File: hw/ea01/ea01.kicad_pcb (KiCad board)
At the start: 2 copper layers, 50 parts, among them J1 Screw_Terminal_01x02, SW1 SW_Push, U1 RP2040, U2 DS1302Z+, U3 NUP2202, U4 MC34063AD, U5 AMS1117-5.0, U6 AMS1117-3.3, U7 MCP601-xOT

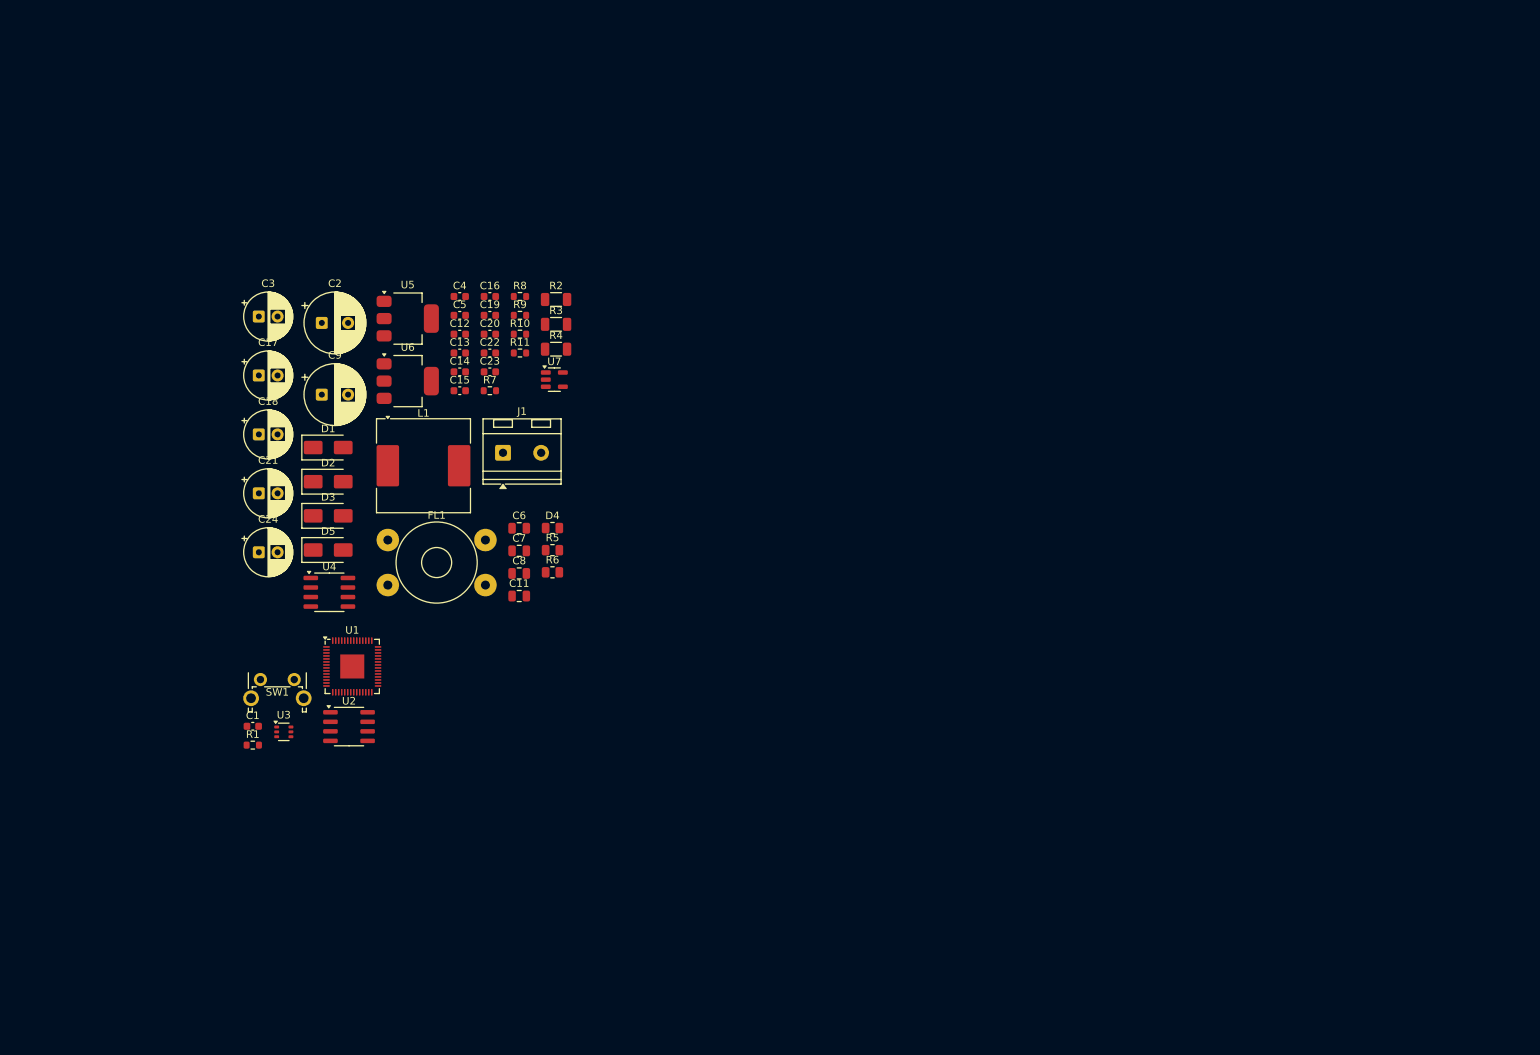
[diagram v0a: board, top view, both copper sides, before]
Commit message: errors fix for comp fp
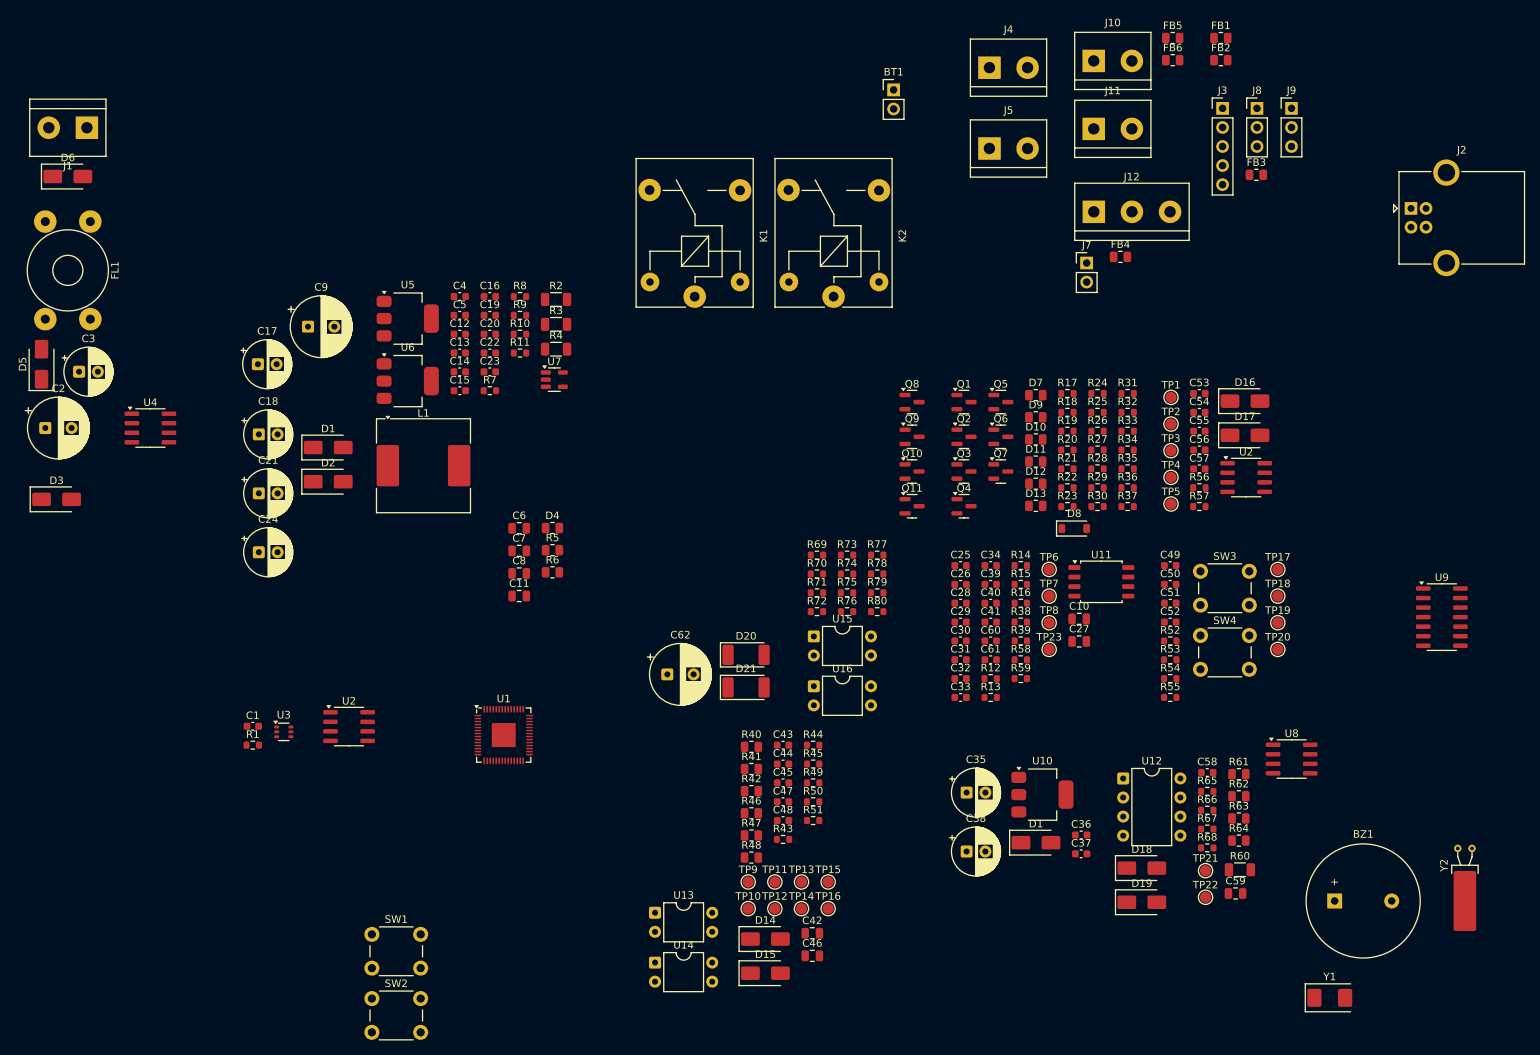
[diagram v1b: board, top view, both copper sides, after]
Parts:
- added BT1: Battery_Cell, Connector_PinHeader_2.54mm:PinHeader_1x02_P2.54mm_Vertical, F.Cu at (199.0, 31.5)
- added BZ1: Buzzer, Buzzer_Beeper:Buzzer_15x7.5RM7.6, F.Cu at (257.8, 139.5)
- added C10: 1uF, Capacitor_SMD:C_0805_2012Metric, F.Cu at (223.7, 101.9)
- added C25: 220nF, Capacitor_SMD:C_0603_1608Metric, F.Cu at (207.9, 94.8)
- added C26: 100nF, Capacitor_SMD:C_0603_1608Metric, F.Cu at (207.9, 97.3)
- added C27: 1uF, Capacitor_SMD:C_0805_2012Metric, F.Cu at (223.7, 104.9)
- added C28: 220nF, Capacitor_SMD:C_0603_1608Metric, F.Cu at (207.9, 99.8)
- added C29: 220nF, Capacitor_SMD:C_0603_1608Metric, F.Cu at (207.9, 102.3)
- added C30: 220nF, Capacitor_SMD:C_0603_1608Metric, F.Cu at (207.9, 104.9)
- added C31: 220nF, Capacitor_SMD:C_0603_1608Metric, F.Cu at (207.9, 107.4)
- added C32: 220nF, Capacitor_SMD:C_0603_1608Metric, F.Cu at (207.9, 109.9)
- added C33: 220nF, Capacitor_SMD:C_0603_1608Metric, F.Cu at (207.9, 112.4)
- added C34: 220nF, Capacitor_SMD:C_0603_1608Metric, F.Cu at (211.9, 94.8)
- added C35: 10uF, Capacitor_THT:CP_Radial_D6.3mm_P2.50mm, F.Cu at (208.7, 125.1)
- added C36: 220nF, Capacitor_SMD:C_0603_1608Metric, F.Cu at (224.0, 130.7)
- added C37: 220nF, Capacitor_SMD:C_0603_1608Metric, F.Cu at (224.0, 133.2)
- added C38: 10uF, Capacitor_THT:CP_Radial_D6.3mm_P2.50mm, F.Cu at (208.7, 132.9)
- added C39: 15pF, Capacitor_SMD:C_0603_1608Metric, F.Cu at (211.9, 97.3)
- added C40: 220nF, Capacitor_SMD:C_0603_1608Metric, F.Cu at (211.9, 99.8)
- added C41: 15pF, Capacitor_SMD:C_0603_1608Metric, F.Cu at (211.9, 102.3)
- added C42: 100nF, Capacitor_SMD:C_0805_2012Metric, F.Cu at (188.2, 143.8)
- added C43: 220nF, Capacitor_SMD:C_0603_1608Metric, F.Cu at (184.3, 118.8)
- added C44: 220nF, Capacitor_SMD:C_0603_1608Metric, F.Cu at (184.3, 121.3)
- added C45: 220nF, Capacitor_SMD:C_0603_1608Metric, F.Cu at (184.3, 123.8)
- added C46: 100nF, Capacitor_SMD:C_0805_2012Metric, F.Cu at (188.2, 146.8)
- added C47: 100nF, Capacitor_SMD:C_0603_1608Metric, F.Cu at (184.3, 126.3)
- added C48: 100nF, Capacitor_SMD:C_0603_1608Metric, F.Cu at (184.3, 128.8)
- added C49: 220nF, Capacitor_SMD:C_0603_1608Metric, F.Cu at (235.8, 94.8)
- added C50: 220nF, Capacitor_SMD:C_0603_1608Metric, F.Cu at (235.8, 97.3)
- added C51: 220nF, Capacitor_SMD:C_0603_1608Metric, F.Cu at (235.8, 99.8)
- added C52: 220nF, Capacitor_SMD:C_0603_1608Metric, F.Cu at (235.8, 102.3)
- added C53: 15pF, Capacitor_SMD:C_0603_1608Metric, F.Cu at (239.7, 71.9)
- added C54: 15pF, Capacitor_SMD:C_0603_1608Metric, F.Cu at (239.7, 74.4)
- added C55: 220nF, Capacitor_SMD:C_0603_1608Metric, F.Cu at (239.7, 76.9)
- added C56: 22pF, Capacitor_SMD:C_0603_1608Metric, F.Cu at (239.7, 79.4)
- added C57: 220nF, Capacitor_SMD:C_0603_1608Metric, F.Cu at (239.7, 81.9)
- added C58: 220nF, Capacitor_SMD:C_0603_1608Metric, F.Cu at (240.8, 122.4)
- added C59: 1uF, Capacitor_SMD:C_0805_2012Metric, F.Cu at (244.6, 138.5)
- added C60: 100nF, Capacitor_SMD:C_0603_1608Metric, F.Cu at (211.9, 104.9)
- added C61: 22pF, Capacitor_SMD:C_0603_1608Metric, F.Cu at (211.9, 107.4)
- added C62: 470uF, Capacitor_THT:CP_Radial_D8.0mm_P3.50mm, F.Cu at (168.9, 109.3)
- added D1: SS26, Diode_SMD:D_SMA, F.Cu at (218.0, 131.7)
- added D10: RED_LED, Resistor_SMD:R_0805_2012Metric, F.Cu at (217.9, 78.0)
- added D11: RED_LED, Resistor_SMD:R_0805_2012Metric, F.Cu at (217.9, 81.0)
- added D12: RED_LED, Resistor_SMD:R_0805_2012Metric, F.Cu at (217.9, 83.9)
- added D13: RED_LED, Resistor_SMD:R_0805_2012Metric, F.Cu at (217.9, 86.9)
- added D14: SMAJ12A, Diode_SMD:D_SMA, F.Cu at (181.9, 144.6)
- added D15: SMAJ12A, Diode_SMD:D_SMA, F.Cu at (181.9, 149.1)
- added D16: SS16, Diode_SMD:D_SMA, F.Cu at (245.8, 72.9)
- added D17: SS16, Diode_SMD:D_SMA, F.Cu at (245.8, 77.5)
- added D18: SMAJ12A, Diode_SMD:D_SMA, F.Cu at (232.1, 135.1)
- added D19: SMAJ12A, Diode_SMD:D_SMA, F.Cu at (232.1, 139.7)
- added D20: SM4007, Diode_SMD:D_MELF, F.Cu at (179.3, 106.7)
- added D21: SM4007, Diode_SMD:D_MELF, F.Cu at (179.3, 111.1)
- added D6: SMAJ24A, Diode_SMD:D_SMA, F.Cu at (89.0, 43.0)
- added D7: RED_LED, Resistor_SMD:R_0805_2012Metric, F.Cu at (217.9, 72.1)
- added D8: 1N4148W, Diode_SMD:D_SOD-123, F.Cu at (223.1, 89.9)
- added D9: RED_LED, Resistor_SMD:R_0805_2012Metric, F.Cu at (217.9, 75.1)
- added FB1: FerriteBead, Resistor_SMD:R_0805_2012Metric, F.Cu at (242.6, 24.6)
- added FB2: FerriteBead, Resistor_SMD:R_0805_2012Metric, F.Cu at (242.6, 27.5)
- added FB3: FerriteBead, Resistor_SMD:R_0805_2012Metric, F.Cu at (247.3, 42.8)
- added FB4: FerriteBead, Resistor_SMD:R_0805_2012Metric, F.Cu at (229.2, 53.7)
- added FB5: FerriteBead, Resistor_SMD:R_0805_2012Metric, F.Cu at (236.2, 24.6)
- added FB6: FerriteBead, Resistor_SMD:R_0805_2012Metric, F.Cu at (236.2, 27.5)
- added J10: Screw_Terminal_01x02, TerminalBlock:TerminalBlock_bornier-2_P5.08mm, F.Cu at (225.7, 27.6)
- added J11: Screw_Terminal_01x02, TerminalBlock:TerminalBlock_bornier-2_P5.08mm, F.Cu at (225.7, 36.6)
- added J12: Screw_Terminal_01x03, TerminalBlock:TerminalBlock_bornier-3_P5.08mm, F.Cu at (225.7, 47.7)
- added J2: USB_B, Connector_USB:USB_B_OST_USB-B1HSxx_Horizontal, F.Cu at (267.9, 47.2)
- added J3: Conn_01x05_Pin, Connector_PinHeader_2.54mm:PinHeader_1x05_P2.54mm_Vertical, F.Cu at (242.8, 33.9)
- added J4: Screw_Terminal_01x02, TerminalBlock:TerminalBlock_bornier-2_P5.08mm, F.Cu at (211.8, 28.5)
- added J5: Screw_Terminal_01x02, TerminalBlock:TerminalBlock_bornier-2_P5.08mm, F.Cu at (211.8, 39.3)
- added J7: Conn_01x02_Pin, Connector_PinHeader_2.54mm:PinHeader_1x02_P2.54mm_Vertical, F.Cu at (224.7, 54.5)
- added J8: Conn_01x03_Pin, Connector_PinHeader_2.54mm:PinHeader_1x03_P2.54mm_Vertical, F.Cu at (247.4, 33.9)
- added J9: Conn_01x03_Pin, Connector_PinHeader_2.54mm:PinHeader_1x03_P2.54mm_Vertical, F.Cu at (252.0, 33.9)
- added K1: SANYOU_SRD_Form_C, Relay_THT:Relay_SPDT_SANYOU_SRD_Series_Form_C, F.Cu at (172.5, 59.0)
- added K2: SANYOU_SRD_Form_C, Relay_THT:Relay_SPDT_SANYOU_SRD_Series_Form_C, F.Cu at (191.0, 59.0)
- added Q1: BC817, Package_TO_SOT_SMD:SOT-23, F.Cu at (208.4, 73.0)
- added Q10: BC817, Package_TO_SOT_SMD:SOT-23, F.Cu at (201.5, 82.3)
- added Q11: BC817, Package_TO_SOT_SMD:SOT-23, F.Cu at (201.5, 86.9)
- added Q2: BC817, Package_TO_SOT_SMD:SOT-23, F.Cu at (208.4, 77.7)
- added Q3: BC817, Package_TO_SOT_SMD:SOT-23, F.Cu at (208.4, 82.3)
- added Q4: BC817, Package_TO_SOT_SMD:SOT-23, F.Cu at (208.4, 86.9)
- added Q5: BC817, Package_TO_SOT_SMD:SOT-23, F.Cu at (213.3, 73.0)
- added Q6: BC817, Package_TO_SOT_SMD:SOT-23, F.Cu at (213.3, 77.7)
- added Q7: BC817, Package_TO_SOT_SMD:SOT-23, F.Cu at (213.3, 82.3)
- added Q8: BC817, Package_TO_SOT_SMD:SOT-23, F.Cu at (201.5, 73.0)
- added Q9: BC817, Package_TO_SOT_SMD:SOT-23, F.Cu at (201.5, 77.7)
- added R12: 22R, Resistor_SMD:R_0603_1608Metric, F.Cu at (211.9, 109.9)
- added R13: 22R, Resistor_SMD:R_0603_1608Metric, F.Cu at (211.9, 112.4)
- added R14: DNF, Resistor_SMD:R_0603_1608Metric, F.Cu at (215.9, 94.8)
- added R15: 1K, Resistor_SMD:R_0603_1608Metric, F.Cu at (215.9, 97.3)
- added R16: 1K, Resistor_SMD:R_0603_1608Metric, F.Cu at (215.9, 99.8)
- added R17: 1K, Resistor_SMD:R_0603_1608Metric, F.Cu at (222.2, 71.9)
- added R18: 100R, Resistor_SMD:R_0603_1608Metric, F.Cu at (222.2, 74.4)
- added R19: 100R, Resistor_SMD:R_0603_1608Metric, F.Cu at (222.2, 76.9)
- added R20: 10K, Resistor_SMD:R_0603_1608Metric, F.Cu at (222.2, 79.4)
- added R21: 100R, Resistor_SMD:R_0603_1608Metric, F.Cu at (222.2, 81.9)
- added R22: 10K, Resistor_SMD:R_0603_1608Metric, F.Cu at (222.2, 84.5)
- added R23: 100R, Resistor_SMD:R_0603_1608Metric, F.Cu at (222.2, 87.0)
- added R24: 10K, Resistor_SMD:R_0603_1608Metric, F.Cu at (226.2, 71.9)
- added R25: 1K, Resistor_SMD:R_0603_1608Metric, F.Cu at (226.2, 74.4)
- added R26: 100R, Resistor_SMD:R_0603_1608Metric, F.Cu at (226.2, 76.9)
- added R27: 10K, Resistor_SMD:R_0603_1608Metric, F.Cu at (226.2, 79.4)
- added R28: 1K, Resistor_SMD:R_0603_1608Metric, F.Cu at (226.2, 81.9)
- added R29: 100R, Resistor_SMD:R_0603_1608Metric, F.Cu at (226.2, 84.5)
- added R30: 10K, Resistor_SMD:R_0603_1608Metric, F.Cu at (226.2, 87.0)
- added R31: 1K, Resistor_SMD:R_0603_1608Metric, F.Cu at (230.2, 71.9)
- added R32: 100R, Resistor_SMD:R_0603_1608Metric, F.Cu at (230.2, 74.4)
- added R33: 10K, Resistor_SMD:R_0603_1608Metric, F.Cu at (230.2, 76.9)
- added R34: 1K, Resistor_SMD:R_0603_1608Metric, F.Cu at (230.2, 79.4)
- added R35: 100R, Resistor_SMD:R_0603_1608Metric, F.Cu at (230.2, 81.9)
- added R36: 10K, Resistor_SMD:R_0603_1608Metric, F.Cu at (230.2, 84.5)
- added R37: 1K, Resistor_SMD:R_0603_1608Metric, F.Cu at (230.2, 87.0)
- added R38: 4.7K, Resistor_SMD:R_0603_1608Metric, F.Cu at (215.9, 102.3)
- added R39: 4.7K, Resistor_SMD:R_0603_1608Metric, F.Cu at (215.9, 104.9)
- added R40: 220R, Resistor_SMD:R_0805_2012Metric, F.Cu at (180.1, 119.0)
- added R41: 10K, Resistor_SMD:R_0805_2012Metric, F.Cu at (180.1, 121.9)
- added R42: 100R, Resistor_SMD:R_0805_2012Metric, F.Cu at (180.1, 124.9)
- added R43: 2.7K, Resistor_SMD:R_0603_1608Metric, F.Cu at (184.3, 131.3)
- added R44: 1K, Resistor_SMD:R_0603_1608Metric, F.Cu at (188.3, 118.8)
- added R45: 1K, Resistor_SMD:R_0603_1608Metric, F.Cu at (188.3, 121.3)
- added R46: 220R, Resistor_SMD:R_0805_2012Metric, F.Cu at (180.1, 127.8)
- added R47: 10K, Resistor_SMD:R_0805_2012Metric, F.Cu at (180.1, 130.8)
- added R48: 100R, Resistor_SMD:R_0805_2012Metric, F.Cu at (180.1, 133.7)
- added R49: 2.7K, Resistor_SMD:R_0603_1608Metric, F.Cu at (188.3, 123.8)
- added R50: 1K, Resistor_SMD:R_0603_1608Metric, F.Cu at (188.3, 126.3)
- added R51: 1K, Resistor_SMD:R_0603_1608Metric, F.Cu at (188.3, 128.8)
- added R52: 2.7K, Resistor_SMD:R_0603_1608Metric, F.Cu at (235.8, 104.9)
- added R53: 1K, Resistor_SMD:R_0603_1608Metric, F.Cu at (235.8, 107.4)
- added R54: 2.7K, Resistor_SMD:R_0603_1608Metric, F.Cu at (235.8, 109.9)
- added R55: 1K, Resistor_SMD:R_0603_1608Metric, F.Cu at (235.8, 112.4)
- added R56: 10K, Resistor_SMD:R_0603_1608Metric, F.Cu at (239.7, 84.5)
- added R57: 1K, Resistor_SMD:R_0603_1608Metric, F.Cu at (239.7, 87.0)
- added R58: 1K, Resistor_SMD:R_0603_1608Metric, F.Cu at (215.9, 107.4)
- added R59: 22R, Resistor_SMD:R_0603_1608Metric, F.Cu at (215.9, 109.9)
- added R60: 120R, Resistor_SMD:R_1206_3216Metric, F.Cu at (245.1, 135.3)
- added R61: 47R, Resistor_SMD:R_0805_2012Metric, F.Cu at (245.0, 122.6)
- added R62: 47R, Resistor_SMD:R_0805_2012Metric, F.Cu at (245.0, 125.6)
- added R63: 4.7K, Resistor_SMD:R_0805_2012Metric, F.Cu at (245.0, 128.5)
- added R64: 4.7K, Resistor_SMD:R_0805_2012Metric, F.Cu at (245.0, 131.5)
- added R65: 10K, Resistor_SMD:R_0603_1608Metric, F.Cu at (240.8, 124.9)
- added R66: 100R, Resistor_SMD:R_0603_1608Metric, F.Cu at (240.8, 127.4)
- added R67: 100R, Resistor_SMD:R_0603_1608Metric, F.Cu at (240.8, 129.9)
- added R68: 100R, Resistor_SMD:R_0603_1608Metric, F.Cu at (240.8, 132.4)
- added R69: 100R, Resistor_SMD:R_0603_1608Metric, F.Cu at (188.8, 93.4)
- added R70: 10K, Resistor_SMD:R_0603_1608Metric, F.Cu at (188.8, 95.9)
- added R71: 100R, Resistor_SMD:R_0603_1608Metric, F.Cu at (188.8, 98.5)
- added R72: 10K, Resistor_SMD:R_0603_1608Metric, F.Cu at (188.8, 101.0)
- added R73: 10K, Resistor_SMD:R_0603_1608Metric, F.Cu at (192.8, 93.4)
- added R74: 100R, Resistor_SMD:R_0603_1608Metric, F.Cu at (192.8, 95.9)
- added R75: 100R, Resistor_SMD:R_0603_1608Metric, F.Cu at (192.8, 98.5)
- added R76: 10K, Resistor_SMD:R_0603_1608Metric, F.Cu at (192.8, 101.0)
- added R77: 10K, Resistor_SMD:R_0603_1608Metric, F.Cu at (196.8, 93.4)
- added R78: 100R, Resistor_SMD:R_0603_1608Metric, F.Cu at (196.8, 95.9)
- added R79: 10K, Resistor_SMD:R_0603_1608Metric, F.Cu at (196.8, 98.5)
- added R80: 100R, Resistor_SMD:R_0603_1608Metric, F.Cu at (196.8, 101.0)
- added SW2: SW_Push, Button_Switch_THT:SW_PUSH_6mm_H5mm, F.Cu at (129.5, 152.5)
- added SW3: SW_Push, Button_Switch_THT:SW_PUSH_6mm_H5mm, F.Cu at (239.9, 95.6)
- added SW4: SW_Push, Button_Switch_THT:SW_PUSH_6mm_H5mm, F.Cu at (239.9, 104.1)
- added TP1: TestPoint, TestPoint:TestPoint_Pad_D1.5mm, F.Cu at (235.9, 72.4)
- added TP10: TestPoint, TestPoint:TestPoint_Pad_D1.5mm, F.Cu at (179.6, 140.5)
- added TP11: TestPoint, TestPoint:TestPoint_Pad_D1.5mm, F.Cu at (183.2, 137.0)
- added TP12: TestPoint, TestPoint:TestPoint_Pad_D1.5mm, F.Cu at (183.2, 140.5)
- added TP13: TestPoint, TestPoint:TestPoint_Pad_D1.5mm, F.Cu at (186.7, 137.0)
- added TP14: TestPoint, TestPoint:TestPoint_Pad_D1.5mm, F.Cu at (186.7, 140.5)
- added TP15: TestPoint, TestPoint:TestPoint_Pad_D1.5mm, F.Cu at (190.3, 137.0)
- added TP16: TestPoint, TestPoint:TestPoint_Pad_D1.5mm, F.Cu at (190.3, 140.5)
- added TP17: TestPoint, TestPoint:TestPoint_Pad_D1.5mm, F.Cu at (250.2, 95.3)
- added TP18: TestPoint, TestPoint:TestPoint_Pad_D1.5mm, F.Cu at (250.2, 98.9)
- added TP19: TestPoint, TestPoint:TestPoint_Pad_D1.5mm, F.Cu at (250.2, 102.4)
- added TP2: TestPoint, TestPoint:TestPoint_Pad_D1.5mm, F.Cu at (235.9, 76.0)
- added TP20: TestPoint, TestPoint:TestPoint_Pad_D1.5mm, F.Cu at (250.2, 106.0)
- added TP21: TestPoint, TestPoint:TestPoint_Pad_D1.5mm, F.Cu at (240.6, 135.5)
- added TP22: TestPoint, TestPoint:TestPoint_Pad_D1.5mm, F.Cu at (240.6, 139.0)
- added TP23: TestPoint, TestPoint:TestPoint_Pad_D1.5mm, F.Cu at (219.7, 106.0)
- added TP3: TestPoint, TestPoint:TestPoint_Pad_D1.5mm, F.Cu at (235.9, 79.5)
- added TP4: TestPoint, TestPoint:TestPoint_Pad_D1.5mm, F.Cu at (235.9, 83.1)
- added TP5: TestPoint, TestPoint:TestPoint_Pad_D1.5mm, F.Cu at (235.9, 86.6)
- added TP6: TestPoint, TestPoint:TestPoint_Pad_D1.5mm, F.Cu at (219.7, 95.3)
- added TP7: TestPoint, TestPoint:TestPoint_Pad_D1.5mm, F.Cu at (219.7, 98.9)
- added TP8: TestPoint, TestPoint:TestPoint_Pad_D1.5mm, F.Cu at (219.7, 102.4)
- added TP9: TestPoint, TestPoint:TestPoint_Pad_D1.5mm, F.Cu at (179.6, 137.0)
- added U10: AMS1117-3.3, Package_TO_SOT_SMD:SOT-223-3_TabPin2, F.Cu at (218.8, 125.3)
- added U11: W25Q32JVSS, Package_SO:SOIC-8_5.3x5.3mm_P1.27mm, F.Cu at (226.7, 97.0)
- added U12: SN75176AP, Package_DIP:DIP-8_W7.62mm, F.Cu at (229.6, 123.2)
- added U13: PC817, Package_DIP:DIP-4_W7.62mm, F.Cu at (167.2, 141.1)
- added U14: PC817, Package_DIP:DIP-4_W7.62mm, F.Cu at (167.2, 147.7)
- added U15: PC817, Package_DIP:DIP-4_W7.62mm, F.Cu at (188.4, 104.3)
- added U16: PC817, Package_DIP:DIP-4_W7.62mm, F.Cu at (188.4, 110.9)
- added U2: PCF8563T, Package_SO:SOIC-8_3.9x4.9mm_P1.27mm, F.Cu at (246.0, 83.1)
- added U8: CAT24C256, Package_SO:SOIC-8_3.9x4.9mm_P1.27mm, F.Cu at (252.0, 120.6)
- added U9: 74HC14, Package_SO:SOIC-14_3.9x8.7mm_P1.27mm, F.Cu at (272.0, 101.7)
- added Y1: 12Mhz, Crystal:Crystal_SMD_Abracon_ABM3-2Pin_5.0x3.2mm, F.Cu at (257.1, 152.4)
- added Y2: 32.768Khz, Crystal:Crystal_C38-LF_D3.0mm_L8.0mm_Horizontal_1EP_style1, F.Cu at (274.1, 132.5)
- J1: footprint TerminalBlock_RND:TerminalBlock_RND_205-00232_1x02_P5.08mm_Horizontal -> TerminalBlock:TerminalBlock_bornier-2_P5.08mm
- SW1: footprint Button_Switch_THT:SW_Tactile_SPST_Angled_PTS645Vx58-2LFS -> Button_Switch_THT:SW_PUSH_6mm_H5mm
- moved J1 70.3 mm to (91.5, 36.5), turned to 180 degrees
- moved FL1 66.5 mm to (86.0, 49.0), turned to -90 degrees
- moved D5 45.5 mm to (85.5, 68.0), turned to 90 degrees
- moved C2 39.4 mm to (86.0, 76.5)
- moved SW1 37.0 mm to (129.5, 143.9)
- moved D3 36.2 mm to (87.5, 86.0)
- moved U4 32.4 mm to (100.0, 76.5)
- moved C3 25.0 mm to (90.5, 69.0)
- moved U1 22.1 mm to (147.1, 117.4)
- moved C9 9.23 mm to (121.0, 63.0)
- moved C17 1.51 mm to (114.3, 68.0)
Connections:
- C1 pad 1: /mcu/iBTN -> /mcu/RUN
- R1 pad 2: /mcu/iBTN -> /mcu/RUN
- SW1 pad 2: /mcu/iBTN -> /mcu/RUN
- U1 pad 1: Net-(U1-IOVDD-Pad1) -> +3.3V
- U1 pad 10: Net-(U1-IOVDD-Pad1) -> +3.3V
- U1 pad 11: unconnected-(U1-GPIO8-Pad11) -> /mcu/UART0_TX
- U1 pad 12: unconnected-(U1-GPIO9-Pad12) -> /mcu/UART0_RX
- U1 pad 15: unconnected-(U1-GPIO12-Pad15) -> RS485_TX
- U1 pad 16: unconnected-(U1-GPIO13-Pad16) -> RS485_RX
- U1 pad 17: unconnected-(U1-GPIO14-Pad17) -> RS485_RW
- U1 pad 18: unconnected-(U1-GPIO15-Pad18) -> BUZZER
- U1 pad 19: unconnected-(U1-TESTEN-Pad19) -> GND
- U1 pad 2: unconnected-(U1-GPIO0-Pad2) -> DIGITAL_IN0
- U1 pad 20: unconnected-(U1-XIN-Pad20) -> Net-(U1-XIN)
- U1 pad 21: unconnected-(U1-XOUT-Pad21) -> Net-(U1-XOUT)
- U1 pad 22: Net-(U1-IOVDD-Pad1) -> +3.3V
- U1 pad 23: Net-(U1-DVDD-Pad23) -> +1.1V
- U1 pad 24: unconnected-(U1-SWCLK-Pad24) -> Net-(J3-Pin_1)
- U1 pad 25: unconnected-(U1-SWD-Pad25) -> Net-(J3-Pin_2)
- U1 pad 26: unconnected-(U1-RUN-Pad26) -> /mcu/RUN
- U1 pad 27: unconnected-(U1-GPIO16-Pad27) -> IN0_LED
- U1 pad 28: unconnected-(U1-GPIO17-Pad28) -> IN1_LED
- U1 pad 29: unconnected-(U1-GPIO18-Pad29) -> RTC_INT
- U1 pad 3: unconnected-(U1-GPIO1-Pad3) -> DIGITAL_IN1
- U1 pad 31: unconnected-(U1-GPIO20-Pad31) -> I2C0_SDA
- U1 pad 32: unconnected-(U1-GPIO21-Pad32) -> I2C0_SCL
- U1 pad 33: Net-(U1-IOVDD-Pad1) -> +3.3V
- U1 pad 36: unconnected-(U1-GPIO24-Pad36) -> OUT1_LED
- U1 pad 37: unconnected-(U1-GPIO25-Pad37) -> OUT0_LED
- U1 pad 38: unconnected-(U1-GPIO26_ADC0-Pad38) -> VIN_MONITOR
- U1 pad 39: unconnected-(U1-GPIO27_ADC1-Pad39) -> /mcu/ADC_TEST
- U1 pad 4: unconnected-(U1-GPIO2-Pad4) -> BUTTON0
- U1 pad 42: Net-(U1-IOVDD-Pad1) -> +3.3V
- U1 pad 43: unconnected-(U1-ADC_AVDD-Pad43) -> Net-(U1-ADC_AVDD)
- U1 pad 44: unconnected-(U1-VREG_IN-Pad44) -> +3.3V
- U1 pad 45: unconnected-(U1-VREG_VOUT-Pad45) -> +1.1V
- U1 pad 46: unconnected-(U1-USB_DM-Pad46) -> /mcu/USB_DM
- U1 pad 47: unconnected-(U1-USB_DP-Pad47) -> /mcu/USP_DP
- U1 pad 48: unconnected-(U1-USB_VDD-Pad48) -> +3.3V
- U1 pad 49: Net-(U1-IOVDD-Pad1) -> +3.3V
- U1 pad 5: unconnected-(U1-GPIO3-Pad5) -> BUTTON1
- U1 pad 50: Net-(U1-DVDD-Pad23) -> +1.1V
- U1 pad 51: unconnected-(U1-QSPI_SD3-Pad51) -> /mcu/QSPI_SD3
- U1 pad 52: unconnected-(U1-QSPI_SCLK-Pad52) -> /mcu/QSPI_SCLK
- U1 pad 53: unconnected-(U1-QSPI_SD0-Pad53) -> /mcu/QSPI_SD0
- U1 pad 54: unconnected-(U1-QSPI_SD2-Pad54) -> /mcu/QSPI_SD2
- U1 pad 55: unconnected-(U1-QSPI_SD1-Pad55) -> /mcu/QSPI_SD1
- U1 pad 56: unconnected-(U1-QSPI_SS-Pad56) -> /mcu/QSPI_SS
- U1 pad 57: unconnected-(U1-GND-Pad57) -> GND
- U1 pad 6: unconnected-(U1-GPIO4-Pad6) -> U_LED1
- U1 pad 7: unconnected-(U1-GPIO5-Pad7) -> U_LED0
- U3 pad 1: unconnected-(U3-Pad1) -> /mcu/USB_D-
- U3 pad 2: unconnected-(U3-Pad2) -> GND
- U3 pad 5: unconnected-(U3-Pad5) -> +5V
- U3 pad 6: unconnected-(U3-Pad6) -> /mcu/UDB_D+

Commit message: pcb drawing continue..
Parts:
- added C63: 100nF, Capacitor_SMD:C_0603_1608Metric, F.Cu at (119.8, 31.0)
- added R81: 4.7K, Resistor_SMD:R_0603_1608Metric, F.Cu at (119.8, 33.5)
- added R82: 4.7K, Resistor_SMD:R_0603_1608Metric, F.Cu at (119.8, 36.0)
- added R83: 4.7K, Resistor_SMD:R_0603_1608Metric, F.Cu at (119.8, 38.5)
- added R84: 4.7K, Resistor_SMD:R_0603_1608Metric, F.Cu at (119.8, 41.0)
- added Y3: 32.768Khz, Crystal:Crystal_C38-LF_D3.0mm_L8.0mm_Horizontal_1EP_style1, F.Cu at (270.8, 22.0)
- K1, K2: value SANYOU_SRD_Form_C -> G5NB; footprint Relay_THT:Relay_SPDT_SANYOU_SRD_Series_Form_C -> Relay_THT:Relay_SPST_Omron_G5NB
- SW1, SW2: footprint Button_Switch_THT:SW_PUSH_6mm_H5mm -> Button_Switch_THT:SW_Tactile_SPST_Angled_PTS645Vx83-2LFS
- moved J11 158.3 mm to (69.5, 62.5), turned to -90 degrees
- moved J10 158.0 mm to (69.5, 52.0), turned to -90 degrees
- moved J4 149.8 mm to (69.5, 75.4), turned to -90 degrees
- moved J5 149.7 mm to (69.5, 86.0), turned to -90 degrees
- moved C42 127.8 mm to (79.5, 76.5)
- moved D14 126.3 mm to (77.5, 73.5)
- moved C46 123.1 mm to (80.5, 87.0)
- moved D15 121.8 mm to (79.0, 84.0)
- moved TP16 120.1 mm to (84.0, 84.5)
- moved BT1 120.0 mm to (104.8, 105.8)
- moved FB1 120.0 mm to (148.3, 98.8)
- moved FB2 120.0 mm to (148.3, 101.8)
- moved FB4 120.0 mm to (135.0, 128.0)
- moved FB5 120.0 mm to (141.9, 98.8)
- moved FB6 120.0 mm to (141.9, 101.8)
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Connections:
- U1 pad 41: unconnected-(U1-GPIO29_ADC3-Pad41) -> /mcu/HW_ADDRESS
- U1 pad 8: unconnected-(U1-GPIO6-Pad8) -> /mcu/HW_VERSION
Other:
- board outline added: 100 x 45 mm

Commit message: component placement continue..
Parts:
- removed BZ1: Buzzer, Buzzer_Beeper:Buzzer_15x7.5RM7.6
- removed C38: 10uF, Capacitor_THT:CP_Radial_D6.3mm_P2.50mm
- removed the D1 at (223.7, 86.2)
- removed D10, D11, D12, D13, D4, D7, D9: RED_LED, Resistor_SMD:R_0805_2012Metric
- removed D3: SMAJ24A, Diode_SMD:D_SMA
- removed FL1: Choke_CommonMode_FerriteCore_1234, Transformer_THT:Transformer_Toroid_Horizontal_D10.5mm_Amidon-T37
- removed J7: Conn_01x02_Pin, Connector_PinHeader_2.54mm:PinHeader_1x02_P2.54mm_Vertical
- removed Q10, Q8: BC817, Package_TO_SOT_SMD:SOT-23
- removed R60: 120R, Resistor_SMD:R_1206_3216Metric
- removed R72, R73, R76, R77: 10K, Resistor_SMD:R_0603_1608Metric
- removed R74, R75: 100R, Resistor_SMD:R_0603_1608Metric
- removed TP10, TP11, TP13, TP15, TP16, TP19, TP2, TP20, TP21, TP22, TP23, TP3, TP4, TP5, TP6, TP7, TP9: TestPoint, TestPoint:TestPoint_Pad_D1.5mm
- removed U15, U16: PC817, Package_DIP:DIP-4_W7.62mm
- removed the U2 at (103.8, 33.2)
- removed Y2: 32.768Khz, Crystal:Crystal_C38-LF_D3.0mm_L8.0mm_Horizontal_1EP_style1
- added C64: 10uF, Capacitor_SMD:C_0805_2012Metric, F.Cu at (75.5, 135.0)
- added J13: Conn_01x02_Pin, Connector_PinHeader_2.54mm:PinHeader_1x02_P2.54mm_Vertical, F.Cu at (274.0, -9.79)
- added J14: Conn_01x02_Pin, Connector_PinHeader_2.54mm:PinHeader_1x02_P2.54mm_Vertical, F.Cu at (200.0, -15.0)
- added J15: Conn_01x02_Pin, Connector_PinHeader_2.54mm:PinHeader_1x02_P2.54mm_Vertical, F.Cu at (219.5, -9.29)
- added J16: Conn_01x02_Pin, Connector_PinHeader_2.54mm:PinHeader_1x02_P2.54mm_Vertical, F.Cu at (83.0, 51.0)
- added J17: Conn_01x02_Pin, Connector_PinHeader_2.54mm:PinHeader_1x02_P2.54mm_Vertical, F.Cu at (89.2, 51.0)
- added J18: Conn_01x02_Pin, Connector_PinHeader_2.54mm:PinHeader_1x02_P2.54mm_Vertical, F.Cu at (258.0, -18.3)
- added J19: Conn_01x02_Pin, Connector_PinHeader_2.54mm:PinHeader_1x02_P2.54mm_Vertical, F.Cu at (112.2, 132.2)
- added J6: Conn_01x02_Pin, Connector_PinHeader_2.54mm:PinHeader_1x02_P2.54mm_Vertical, F.Cu at (141.2, -12.4)
- C10, C11, C25, C26, C27, C28, C29, C30, C31, C32, C33, C34, C36, C37, C4, C5, D14, D15, D18, D19, D20, D21, FB3, R5, R59, R6, U10: moved to B.Cu
- C17, C18, C21: footprint Capacitor_THT:CP_Radial_D6.3mm_P2.50mm -> Capacitor_SMD:C_0805_2012Metric
- C24, C35: footprint Capacitor_THT:CP_Radial_D6.3mm_P2.50mm -> Capacitor_SMD:C_0805_2012Metric; moved to B.Cu
- C3: value 100uF -> 10uF; footprint Capacitor_THT:CP_Radial_D6.3mm_P2.50mm -> Capacitor_SMD:C_0805_2012Metric
- D1: value SMAJ24A -> SS26; moved to B.Cu
- moved U9 167.4 mm to (110.5, 61.8), turned to 180 degrees
- moved C63 159.4 mm to (227.1, 148.9)
- moved R81 159.4 mm to (227.1, 151.4)
- moved R83 159.4 mm to (227.1, 156.5)
- moved R84 159.4 mm to (227.1, 159.0)
- moved C1 159.4 mm to (198.3, 151.2)
- moved R1 159.4 mm to (198.3, 153.7)
- moved R82 159.4 mm to (227.1, 153.9)
- moved R64 153.5 mm to (97.2, 83.7), turned to -90 degrees
- moved R62 151.5 mm to (99.2, 83.7), turned to 90 degrees
- moved R61 149.1 mm to (101.8, 83.7), turned to -90 degrees
- moved D18 147.5 mm to (90.5, 82.2), turned to 90 degrees
- moved R63 147.0 mm to (103.8, 83.7), turned to -90 degrees
- moved D19 144.3 mm to (94.0, 82.2), turned to 90 degrees
- moved Y1 138.0 mm to (129.2, 72.2), turned to 180 degrees
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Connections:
- C18 pad 1: 5V -> +3.3V
- C24 pad 1: +3.3V -> Net-(D1-A)
- D1 pad 1: GND -> +3.3V
- D1 pad 2: GND -> Net-(D1-A)
- D6 pad 1: Net-(D6-A1) -> Net-(D5-A)
- D6 pad 2: Net-(D6-A2) -> GND
- J1 pad 1: Net-(D6-A2) -> GND
- J1 pad 2: Net-(D6-A1) -> Net-(D5-A)
- R69 pad 1: Net-(R69-Pad1) -> OUT0
- R78 pad 1: Net-(R78-Pad1) -> OUT1
- U1 pad 34: unconnected-(U1-GPIO22-Pad34) -> OUT1
- U1 pad 35: unconnected-(U1-GPIO23-Pad35) -> OUT0
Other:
- board text added: "Buzzer"
- board text added: "IN_LED0"
- board text added: "IN_LED1"
- board text added: "OUT_LED0"
- board text added: "OUT_LED1"
- board text added: "RTC"
- board text added: "U_LED0"
- board text added: "U_LED1"

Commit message: placement continue...
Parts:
- removed C14, C15, C16, C37: 220nF, Capacitor_SMD:C_0603_1608Metric
- removed C24: 10uF, Capacitor_SMD:C_0805_2012Metric
- removed C56: 22pF, Capacitor_SMD:C_0603_1608Metric
- removed D1: SS26, Diode_SMD:D_SMA
- removed R10, R7, R8: 10K, Resistor_SMD:R_0603_1608Metric
- removed R9: 100R, Resistor_SMD:R_0603_1608Metric
- removed TP1, TP12, TP14, TP17, TP18, TP8: TestPoint, TestPoint:TestPoint_Pad_D1.5mm
- removed U10: AMS1117-3.3, Package_TO_SOT_SMD:SOT-223-3_TabPin2
- removed U7: MCP601-xOT, Package_TO_SOT_SMD:SOT-23-5
- added J7: Conn_01x03_Pin, Connector_PinHeader_2.54mm:PinHeader_1x03_P2.54mm_Vertical, F.Cu at (158.5, 70.5)
- C57, C63, D6, D8, Q1, R18, R19, R20, R57, R65, R66, R67, R68, R81, R82, R83, R84, Y3: moved to B.Cu
- D16, D17: footprint Diode_SMD:D_SMA -> Diode_SMD:D_MiniMELF; moved to B.Cu
- J13, J14, J15, J16, J17, J18, J19, J6: footprint Connector_PinHeader_2.54mm:PinHeader_1x02_P2.54mm_Vertical -> Connector_PinHeader_1.27mm:PinHeader_1x02_P1.27mm_Vertical
- moved J13 185.8 mm to (98.5, 51.4)
- moved J18 177.0 mm to (95.2, 51.4)
- moved R84 160.4 mm to (108.5, 51.0), turned to 90 degrees
- moved R83 157.6 mm to (110.0, 51.0), turned to -90 degrees
- moved R81 157.5 mm to (105.8, 51.0), turned to -90 degrees
- moved C63 157.1 mm to (104.2, 51.0), turned to 90 degrees
- moved R67 148.9 mm to (98.2, 70.5), turned to -90 degrees
- moved J15 147.1 mm to (85.5, 51.4)
- moved R65 147.0 mm to (99.8, 70.5), turned to -90 degrees
- moved R66 144.2 mm to (102.8, 70.5), turned to 90 degrees
- moved R68 143.2 mm to (104.2, 70.5), turned to 90 degrees
- moved Q2 143.0 mm to (118.9, 42.0)
- moved Q3 143.0 mm to (133.5, 42.8)
- moved R24 143.0 mm to (132.2, 37.8)
- moved R25 143.0 mm to (136.7, 41.2)
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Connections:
- net 5V renamed +5V_REG
- C45 pad 2: unconnected-(C45-Pad2) -> GND
- U2 pad 7: Net-(U2-CLKO) -> unconnected-(U2-CLKO-Pad7)
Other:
- board text removed: "Buzzer"
- board text removed: "OUT_LED0"
- board text removed: "OUT_LED1"
- board text removed: "RTC"

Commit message: placement optimization and review continue
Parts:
- added R7: 4.7K, Resistor_SMD:R_0603_1608Metric, B.Cu at (120.8, 51.2)
- added R8: 4.7K, Resistor_SMD:R_0603_1608Metric, B.Cu at (119.2, 51.2)
- C18, C21, C22, C23, C58, C59, Q3, Q5, Q7, R14, R15, R24, R30, R36: moved to B.Cu
- moved R50 62.0 mm to (102.8, 64.0), turned to 90 degrees
- moved C47 58.0 mm to (104.2, 64.0), turned to -90 degrees
- moved C58 52.8 mm to (102.8, 77.8), turned to 90 degrees
- moved C59 46.2 mm to (104.8, 77.8), turned to 90 degrees
- moved R26 39.1 mm to (121.2, 69.5), turned to 180 degrees
- moved C23 36.0 mm to (142.0, 77.8), turned to -90 degrees
- moved R24 35.8 mm to (102.8, 58.2), turned to 90 degrees
- moved R35 34.0 mm to (138.2, 60.2), turned to 90 degrees
- moved R29 33.6 mm to (121.2, 71.0), turned to 180 degrees
- moved R23 33.3 mm to (121.2, 68.0), turned to 180 degrees
- moved Q3 32.0 mm to (105.5, 58.2)
- moved R32 31.4 mm to (136.8, 60.2), turned to 90 degrees
- moved C18 30.5 mm to (144.0, 77.8), turned to -90 degrees
- moved C21 29.9 mm to (144.0, 81.5), turned to 90 degrees
- moved C22 29.7 mm to (142.0, 81.5), turned to 90 degrees
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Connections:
- net /mcu/HW_VERSION renamed /mcu/HW_VER0
- U1 pad 9: unconnected-(U1-GPIO7-Pad9) -> /mcu/HW_VER1
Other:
- board text removed: "IN_LED0"
- board text removed: "IN_LED1"
- board text removed: "U_LED0"
- board text removed: "U_LED1"

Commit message: placement completed.
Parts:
- removed C17, C64: 10uF, Capacitor_SMD:C_0805_2012Metric
- removed C19, C20: 220nF, Capacitor_SMD:C_0603_1608Metric
- removed U5: AMS1117-5.0, Package_TO_SOT_SMD:SOT-223-3_TabPin2
- moved J1 5.08 mm to (137.8, 89.8), turned to 0 degrees
- moved C45 3.04 mm to (107.7, 67.8)
- moved U9 3.04 mm to (113.2, 64.0)
- moved J10 0.74 mm to (69.7, 53.2)
- moved J4 0.74 mm to (69.7, 74.2)
- moved J5 0.73 mm to (69.7, 84.8)
- moved J11 0.70 mm to (69.7, 63.7)
- moved BT1 0.44 mm to (151.6, 64.9)
- moved Y3 0.35 mm to (138.9, 66.3)
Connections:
- C11 pad 1: +6.8V -> +5V_REG
- C12 pad 1: +6.8V -> +5V_REG
- C13 pad 1: +6.8V -> +5V_REG
- C9 pad 1: +6.8V -> +5V_REG
- D8 pad 1: +6.8V -> +5V
- J1 pad 1: GND -> Net-(D5-A)
- J1 pad 2: Net-(D5-A) -> GND
- J6 pad 2: +6.8V -> +5V
- L1 pad 2: +6.8V -> +5V_REG
- R6 pad 1: +6.8V -> +5V_REG
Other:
- outline, holes or cut-outs redrawn
- board text added: "G R T"
